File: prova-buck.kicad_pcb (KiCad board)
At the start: 4 copper layers, 42 x 18 mm, 21 parts, among them J1 Screw_Terminal_01x02, J2 Screw_Terminal_01x02, U1 MPQ9841GL

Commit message: "second commit"
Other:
- net class Default removed

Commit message: "Updated project"
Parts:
- J1, J2: footprint TerminalBlock:TerminalBlock_bornier-2_P5.08mm -> TerminalBlock_Phoenix:TerminalBlock_Phoenix_MPT-0,5-2-2.54_1x02_P2.54mm_Horizontal
- R3: value 33k -> 169k
- U1: value MPQ9841GL -> MPQ9842GL; footprint buck_foot_lib:QFN16_3mm_x_4mm -> buck_foot_lib:MPQ9842GL-Z
- moved C1 1.53 mm to (138.0, 72.5)
- moved C2 1.52 mm to (138.0, 67.8)
- moved J1 1.25 mm to (131.0, 72.8)
- moved C4 1.00 mm to (140.5, 68.5)
- moved C5 1.00 mm to (140.5, 72.0)
- moved C8 0.75 mm to (148.2, 64.5)
- moved C9 0.75 mm to (143.0, 64.5)
- moved R3 0.75 mm to (141.2, 64.5)
- moved R4 0.75 mm to (144.8, 64.5)
- moved R5 0.75 mm to (146.5, 64.5)
- moved C7 0.50 mm to (148.2, 75.5)
- moved R1 0.50 mm to (142.2, 75.5)
- moved R2 0.50 mm to (144.2, 75.5)
- moved R6 0.50 mm to (146.2, 75.5)
- moved C3 0.25 mm to (150.0, 64.5)
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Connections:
- C6 pad 2: /SW -> Net-(C6-Pad2)
- L1 pad 1: /SW -> Net-(C6-Pad2)
- U1 pad 10: /SW -> Net-(C6-Pad2)
- U1 pad 3: /SW -> unconnected-(U1-Pad3)
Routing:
- net /Vout: track 0.00 -> 24.8 mm, vias 0 -> 13
- net /Vcc: track 5.99 -> 18.0 mm, vias 0 -> 2
- net VDD: track 0.00 -> 11.9 mm, vias 0 -> 8
- net GND: track 0.00 -> 6.80 mm, vias 0 -> 27
- net /FB: track 3.17 -> 6.78 mm
- net /SS: track 4.78 -> 5.77 mm
- added copper zone on F.Cu, net /Vout
- added copper zone on F.Cu, net GND
- added copper zone on F.Cu, net Net-(C6-Pad2)
- added copper zone on F.Cu, net VDD

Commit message: "Added Inductor, Buck 3d models"
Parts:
- L1: value 2.2u -> 10u
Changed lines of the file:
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@@
       (effects (font (size 1 1) (thickness 0.15)))
     )
-    (fp_text value "2.2u" (at 0 4.1) (layer "F.Fab")
+    (fp_text value "10u" (at 0 4.1) (layer "F.Fab")
       (effects (font (size 1 1) (thickness 0.15)))
     )
@@
     (pad "2" smd rect locked (at 2.05 0) (size 1.9 2.5) (layers "F.Cu" "F.Paste" "F.Mask")
       (net 11 "/Vout") (pintype "passive"))
-    (model "${KISYS3DMOD}/Inductor_SMD.3dshapes/L_Sunlord_MWSA0518.wrl"
+    (model "${KIPRJMOD}/Cads/User Library-mwsa0503.step"
       (offset (xyz 0 0 0))
       (scale (xyz 1 1 1))

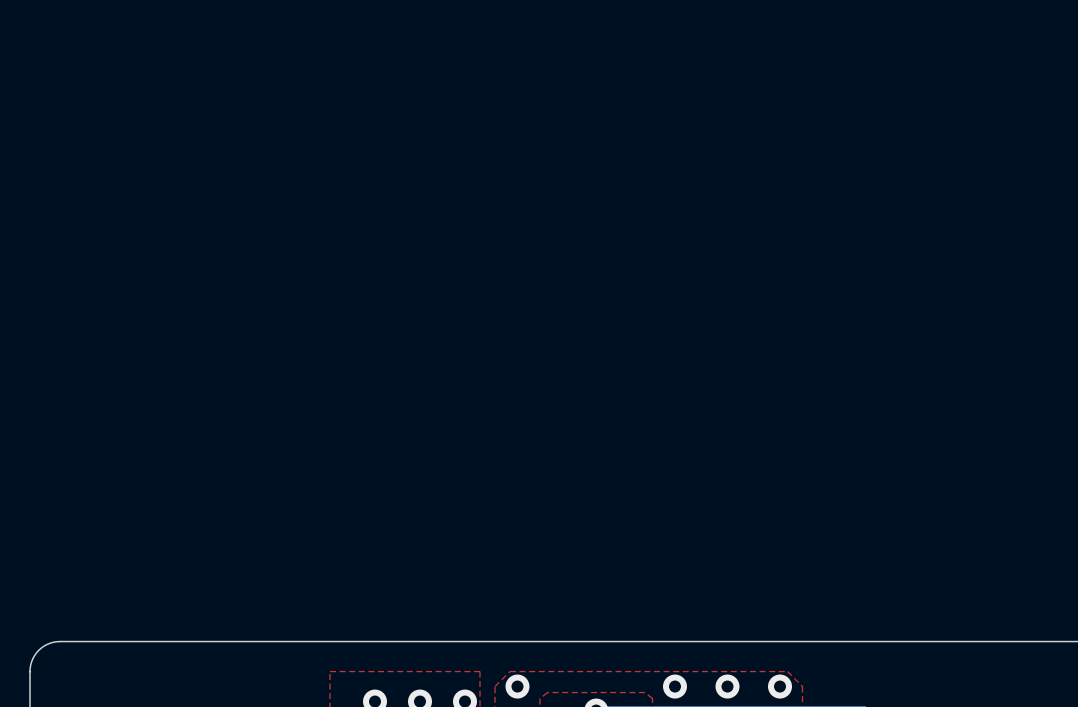
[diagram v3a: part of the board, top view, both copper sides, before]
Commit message: " Added power supply selector"
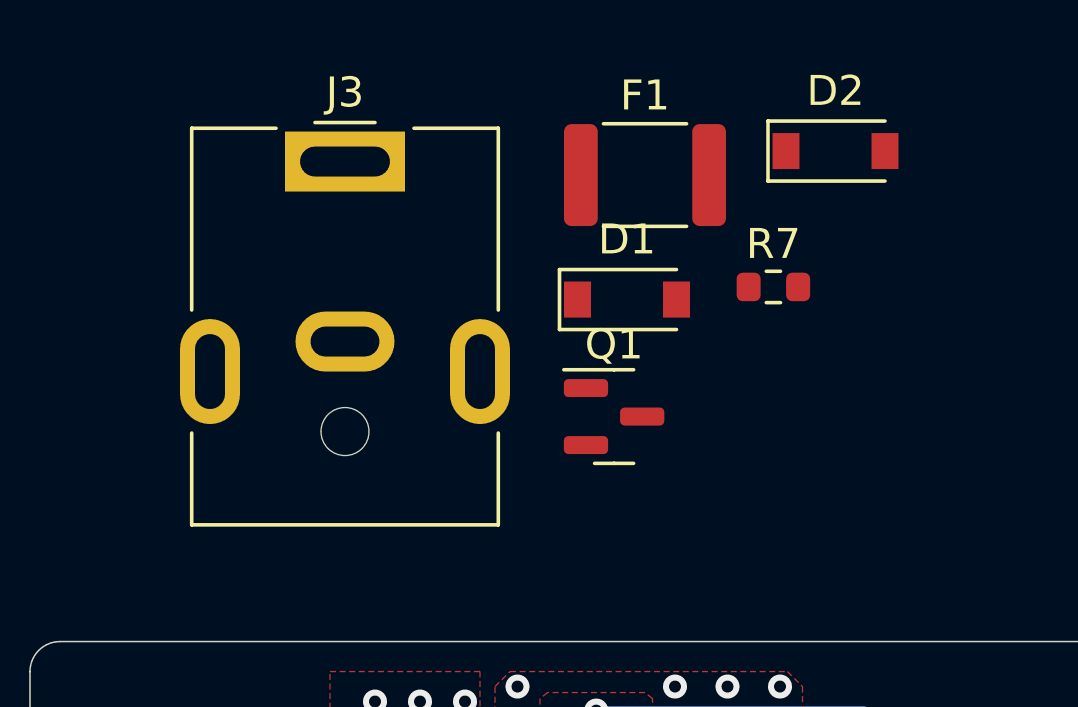
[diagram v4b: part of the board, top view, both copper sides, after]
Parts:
- added D1: D_Schottky_Small, Diode_SMD:D_SOD-123, F.Cu at (144.9, 49.6)
- added D2: D_Zener_Small, Diode_SMD:D_SOD-123, F.Cu at (151.8, 44.6)
- added F1: Polyfuse_Small, Fuse:Fuse_1812_4532Metric, F.Cu at (145.5, 45.5)
- added J3: Jack-DC, Connector_BarrelJack:BarrelJack_CUI_PJ-063AH_Horizontal, F.Cu at (135.5, 45.0)
- added Q1: AO3401A, Package_TO_SOT_SMD:SOT-23, F.Cu at (144.5, 53.5)
- added R7: R_Small, Resistor_SMD:R_0603_1608Metric, F.Cu at (149.8, 49.2)
- L1: value 10u -> 2.2u
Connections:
- J1 pad 2: VDD -> Net-(J1-Pad2)

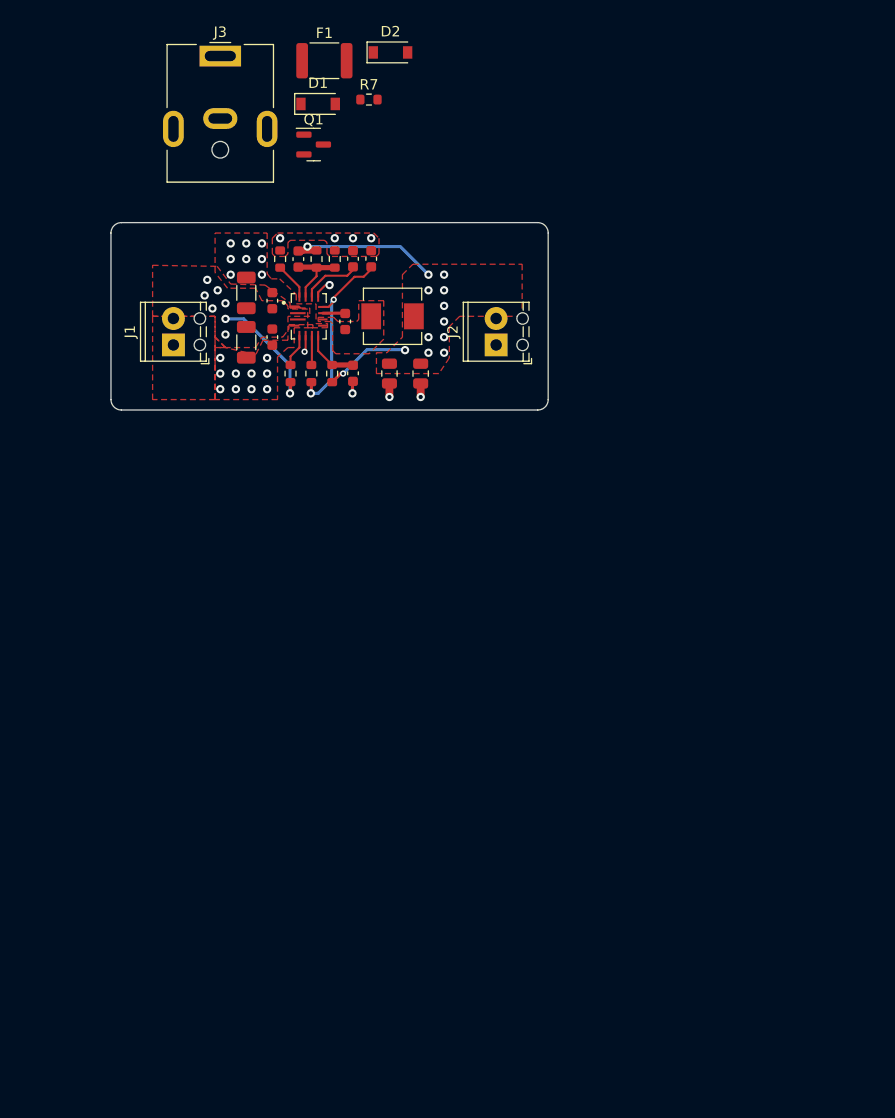
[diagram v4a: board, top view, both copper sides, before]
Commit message: "added LDO"
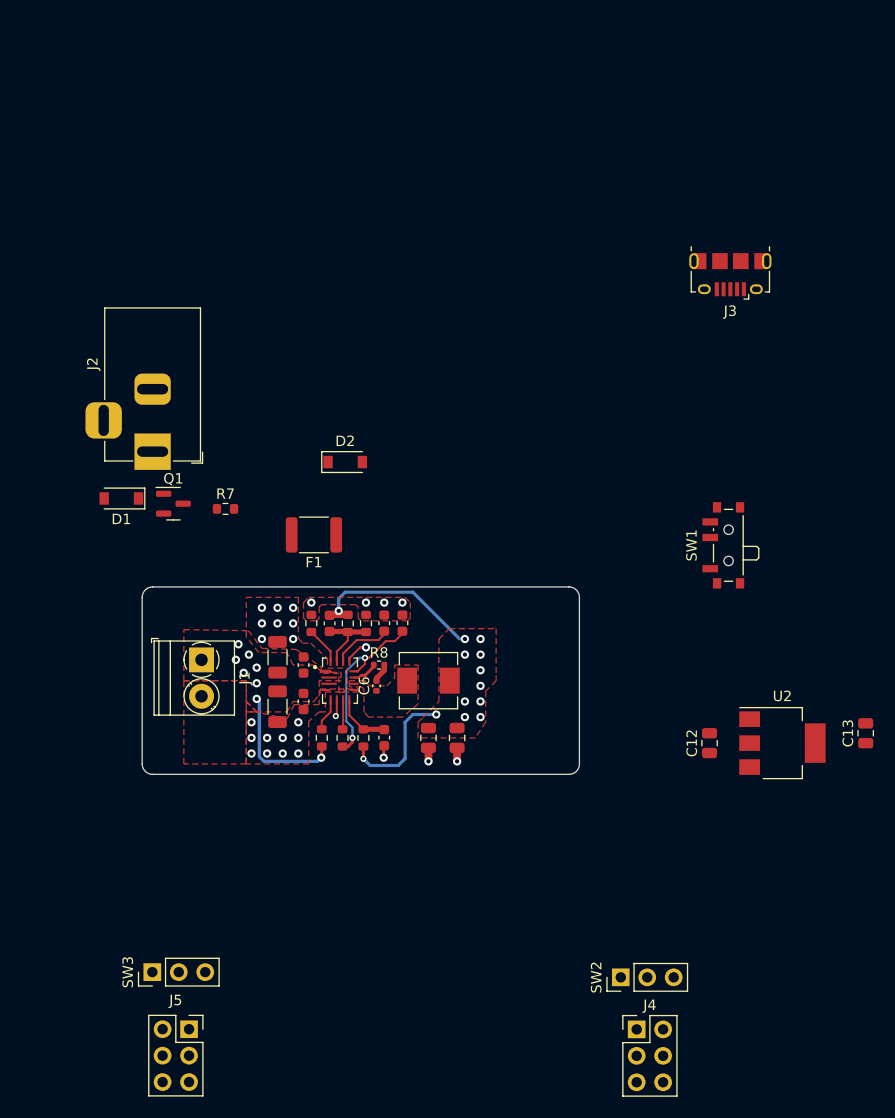
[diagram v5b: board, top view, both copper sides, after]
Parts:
- added C12: 1u, Capacitor_SMD:C_0805_2012Metric, F.Cu at (182.5, 111.0)
- added C13: 4.7u, Capacitor_SMD:C_0805_2012Metric, F.Cu at (197.5, 110.0)
- added J4: Conn_02x03_Counter_Clockwise, Connector_PinHeader_2.54mm:PinHeader_2x03_P2.54mm_Vertical, F.Cu at (175.5, 138.5)
- added J5: Conn_02x03_Counter_Clockwise, Connector_PinSocket_2.54mm:PinSocket_2x03_P2.54mm_Vertical, F.Cu at (132.5, 138.5)
- added R8: 10, Resistor_SMD:R_0402_1005Metric, F.Cu at (150.8, 103.5)
- added SW1: SW_SPDT, Button_Switch_SMD:SW_SPDT_PCM12, F.Cu at (184.0, 92.0)
- added SW2: SW_SPDT, Connector_PinHeader_2.54mm:PinHeader_1x03_P2.54mm_Vertical, F.Cu at (174.0, 133.5)
- added SW3: SW_SPDT, Connector_PinHeader_2.54mm:PinHeader_1x03_P2.54mm_Vertical, F.Cu at (129.0, 133.0)
- added U2: LDL1117S33R, Package_TO_SOT_SMD:SOT-223-3_TabPin2, F.Cu at (189.5, 111.0)
- C6: footprint Capacitor_SMD:C_0603_1608Metric -> Capacitor_SMD:C_0402_1005Metric
- J1: footprint TerminalBlock_Phoenix:TerminalBlock_Phoenix_MPT-0,5-2-2.54_1x02_P2.54mm_Horizontal -> TerminalBlock_Phoenix:TerminalBlock_Phoenix_PT-1,5-2-3.5-H_1x02_P3.50mm_Horizontal
- J2: value Screw_Terminal_01x02 -> Barrel_Jack; footprint TerminalBlock_Phoenix:TerminalBlock_Phoenix_MPT-0,5-2-2.54_1x02_P2.54mm_Horizontal -> Connector_BarrelJack:BarrelJack_Horizontal
- J3: value Jack-DC -> USB_B_Micro; footprint Connector_BarrelJack:BarrelJack_CUI_PJ-063AH_Horizontal -> Connector_USB:USB_Micro-B_Amphenol_10118194_Horizontal
- moved J3 53.3 mm to (184.5, 66.0), turned to 180 degrees
- moved F1 45.6 mm to (144.5, 91.0), turned to 180 degrees
- moved D1 42.4 mm to (126.0, 87.5), turned to 180 degrees
- moved R7 41.7 mm to (136.0, 88.5)
- moved D2 39.6 mm to (147.5, 84.0)
- moved Q1 37.0 mm to (131.0, 88.0)
- moved C10 35.2 mm to (155.5, 110.5)
- moved C11 35.2 mm to (158.2, 110.5)
- moved L1 35.2 mm to (155.5, 105.0)
- moved C1 35.1 mm to (141.0, 107.5)
- moved C2 35.1 mm to (141.0, 102.8)
- moved C3 35.1 mm to (153.0, 99.5)
- moved C4 35.1 mm to (143.5, 103.5)
- moved C5 35.1 mm to (143.5, 107.0)
- moved C6 35.1 mm to (150.5, 105.5), turned to 90 degrees
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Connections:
- C6 pad 1: /BST -> /SW
- C6 pad 2: Net-(C6-Pad2) -> /Rboost
- J2 pad 1: GND -> Net-(D1-Pad2)
- J2 pad 2: /Vout -> GND
- J3 pad 1: Net-(D1-Pad2) -> VBUS
- J3 pad 2: GND -> unconnected-(J3-Pad2)
- L1 pad 1: Net-(C6-Pad2) -> /SW
- U1 pad 10: Net-(C6-Pad2) -> /SW
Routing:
- net /Vout: track 24.8 -> 31.3 mm
- net /Rboost: track 0.00 -> 1.83 mm
- net VDD: track 11.9 -> 13.0 mm
- net GND: track 6.80 -> 7.70 mm
- net /Vcc: track 18.0 -> 17.2 mm
- added copper zone on F.Cu, net /SW
- removed copper zone on F.Cu, net Net-(C6-Pad2)

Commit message: "added JLCPB and Mouser components"
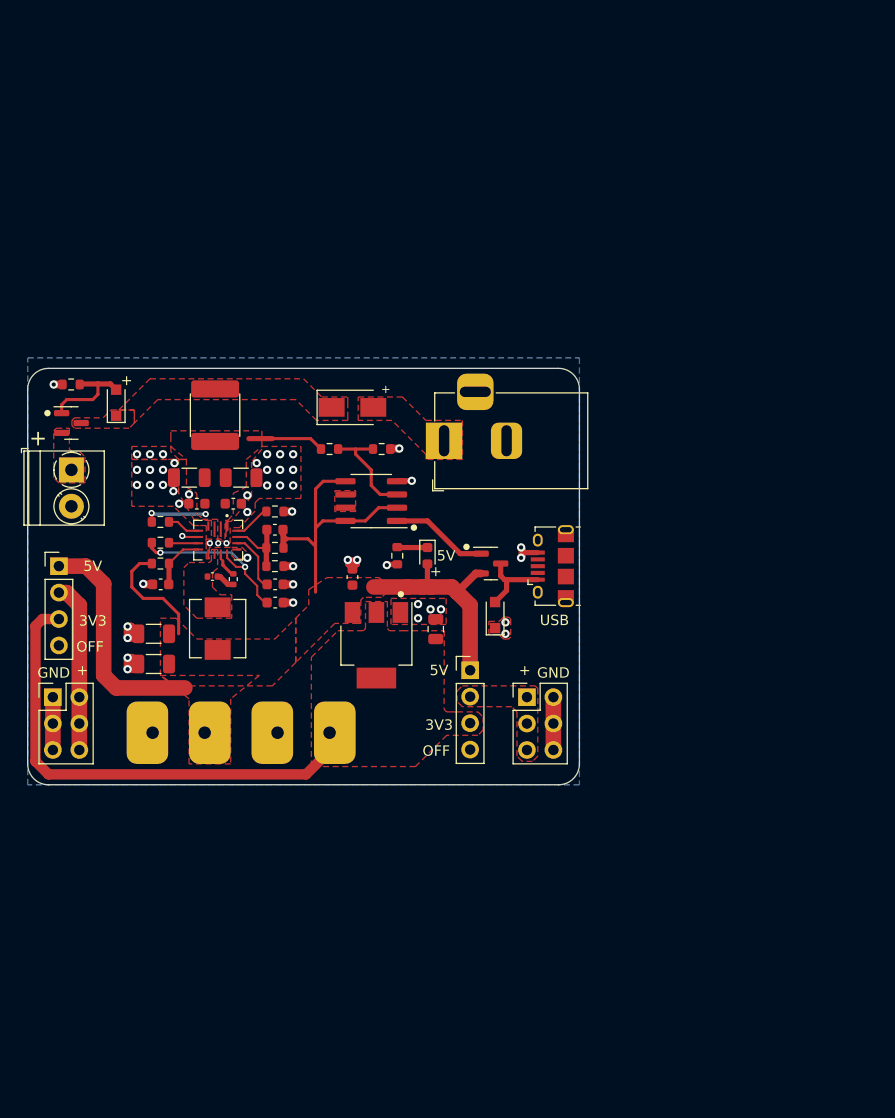
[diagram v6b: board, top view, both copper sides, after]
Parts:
- removed SW1: SW_SPDT, Button_Switch_SMD:SW_SPDT_PCM12
- removed SW2, SW3: SW_SPDT, Connector_PinHeader_2.54mm:PinHeader_1x03_P2.54mm_Vertical
- added D3: BLUE, LED_SMD:LED_0603_1608Metric, F.Cu at (155.4, 93.0)
- added D4: D_TVS, Diode_SMD:D_SOD-323_HandSoldering, F.Cu at (161.9, 98.7)
- added J6: Conn_01x04, Connector_PinHeader_2.54mm:PinHeader_1x04_P2.54mm_Vertical, F.Cu at (159.5, 104.0)
- added J7: Conn_01x04, Connector_PinHeader_2.54mm:PinHeader_1x04_P2.54mm_Vertical, F.Cu at (120.0, 94.0)
- added J8: Conn_01x02, buck_foot_lib:Solder_wire_PAD, F.Cu at (131.5, 110.0)
- added J9: Conn_01x02, buck_foot_lib:Solder_wire_PAD, F.Cu at (143.5, 110.0)
- added Q2: AO3401A, Package_TO_SOT_SMD:SOT-23, F.Cu at (161.5, 93.8)
- added R10: 22k, Resistor_SMD:R_0603_1608Metric, F.Cu at (151.0, 82.8)
- added R11: 820, Resistor_SMD:R_0603_1608Metric, F.Cu at (152.5, 93.0)
- added R9: 5.6k, Resistor_SMD:R_0603_1608Metric, F.Cu at (146.0, 82.8)
- added U3: LM358, Package_SO:SOIC-8_3.9x4.9mm_P1.27mm, F.Cu at (150.0, 87.8)
- C10, C11: footprint Capacitor_SMD:C_0805_2012Metric -> Capacitor_SMD:C_1206_3216Metric
- C12: value 1u -> 2.2u; footprint Capacitor_SMD:C_0805_2012Metric -> Capacitor_SMD:C_0603_1608Metric
- D1: footprint Diode_SMD:D_SOD-123 -> Diode_SMD:D_SMA
- D2: value D_Zener_Small -> UDZVFH10B; footprint Diode_SMD:D_SOD-123 -> Diode_SMD:D_SOD-323_HandSoldering
- F1: footprint Fuse:Fuse_1812_4532Metric -> Fuse:Fuse_2016_HandSolder
- J2: value Barrel_Jack -> Barrel_Jack_MountingPin
- J4: value Conn_02x03_Counter_Clockwise -> Conn_02x03_Odd_Even
- J5: value Conn_02x03_Counter_Clockwise -> Conn_02x03_Odd_Even; footprint Connector_PinSocket_2.54mm:PinSocket_2x03_P2.54mm_Vertical -> Connector_PinHeader_2.54mm:PinHeader_2x03_P2.54mm_Vertical
- L1: value 2.2u -> 10u
- R3: value 169k -> 82k
- R4: value 68.1k -> 68k
- R7: value R_Small -> 47k
- U1: footprint buck_foot_lib:MPQ9842GL-Z -> buck_foot_lib:QFN16_3mm_x_4mm
- moved C13 42.5 mm to (156.2, 100.0)
- moved U2 40.1 mm to (150.5, 101.6), turned to -90 degrees
- moved C12 37.8 mm to (148.2, 95.0)
- moved J5 34.5 mm to (119.4, 106.6)
- moved J4 33.6 mm to (165.0, 106.6)
- moved J3 32.8 mm to (167.4, 94.0), turned to 90 degrees
- moved C11 30.0 mm to (129.1, 103.4), turned to 180 degrees
- moved C10 28.2 mm to (129.1, 100.5), turned to 180 degrees
- moved J2 28.0 mm to (157.0, 82.0), turned to 180 degrees
- moved C7 26.0 mm to (129.8, 95.8), turned to 0 degrees
- moved R1 25.9 mm to (129.8, 89.8), turned to 0 degrees
- moved R6 25.7 mm to (129.8, 93.8), turned to 180 degrees
- moved R2 25.6 mm to (129.8, 91.8), turned to 180 degrees
- moved D1 23.9 mm to (148.2, 78.8), turned to 0 degrees
- moved C1 23.6 mm to (132.5, 85.5), turned to 180 degrees
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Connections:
- net Net-(D1-Pad2) renamed /Vjack
- C10 pad 1: /Vout -> +5V
- C11 pad 1: /Vout -> +5V
- C9 pad 2: /Vout -> +5V
- J1 pad 1: GND -> /Vbat
- J1 pad 2: Net-(J1-Pad2) -> GND
- J3 pad 6: GND -> unconnected-(J3-Pad6)
- J4 pad 1: Net-(J4-Pad1) -> Vleft
- J4 pad 2: Net-(J4-Pad1) -> GND
- J4 pad 3: Net-(J4-Pad1) -> Vleft
- J4 pad 5: GND -> Vleft
- J5 pad 1: Net-(J5-Pad1) -> GND
- J5 pad 2: Net-(J5-Pad1) -> Vright
- J5 pad 3: Net-(J5-Pad1) -> GND
- J5 pad 4: GND -> Vright
- J5 pad 6: GND -> Vright
- L1 pad 2: /Vout -> +5V
- Q1 pad 2: Net-(J1-Pad2) -> /Vbat
- R4 pad 2: /Vout -> +5V
- R6 pad 2: /Vout -> +5V
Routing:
- net +5V: track 0.00 -> 84.1 mm
- net +3V3: track 0.00 -> 47.2 mm
- net /Vout: track 31.3 -> 0.00 mm, vias 13 -> 0
- net GND: track 7.70 -> 38.0 mm, vias 27 -> 53
- net Vright: track 0.00 -> 16.4 mm
- net /Vcomp+: track 0.00 -> 10.3 mm
- net Net-(D2-Pad2): track 0.00 -> 9.44 mm
- net /Vusb_En: track 0.00 -> 9.39 mm
- net VBUS: track 0.00 -> 7.51 mm
- net Net-(D3-Pad1): track 0.00 -> 2.92 mm
- net VDD: track 13.0 -> 13.4 mm, vias 8 -> 2
- added copper zone on F.Cu, net +3V3
- added copper zone on F.Cu, net +5V
- added copper zone on F.Cu, net /UNUSED
- added copper zone on F.Cu, net /Vbat
- added copper zone on F.Cu, net /Vjack
- added copper zone on B.Cu, net GND
- added copper zone on F.Cu, net VDC
- added copper zone on F.Cu, net Vleft
- removed copper zone on F.Cu, net /Vout
- removed copper zone on In1.Cu, net GND
- removed copper zone on In2.Cu, net GND
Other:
- board size 42 x 18 mm -> 53 x 40 mm
- copper layers 4 -> 2
- board text added: "+"
- board text added: "3V3"
- board text added: "5V"
- board text added: "GND"
- board text added: "OFF"
- board text added: "USB"
